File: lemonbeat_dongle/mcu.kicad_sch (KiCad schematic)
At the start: 43 parts, among them J201 USB_A, J202 Prog, J203 u.FL, SW201 SW_Push, U201 nRF52840, Y201 32MHz, Y202 32.768kHz

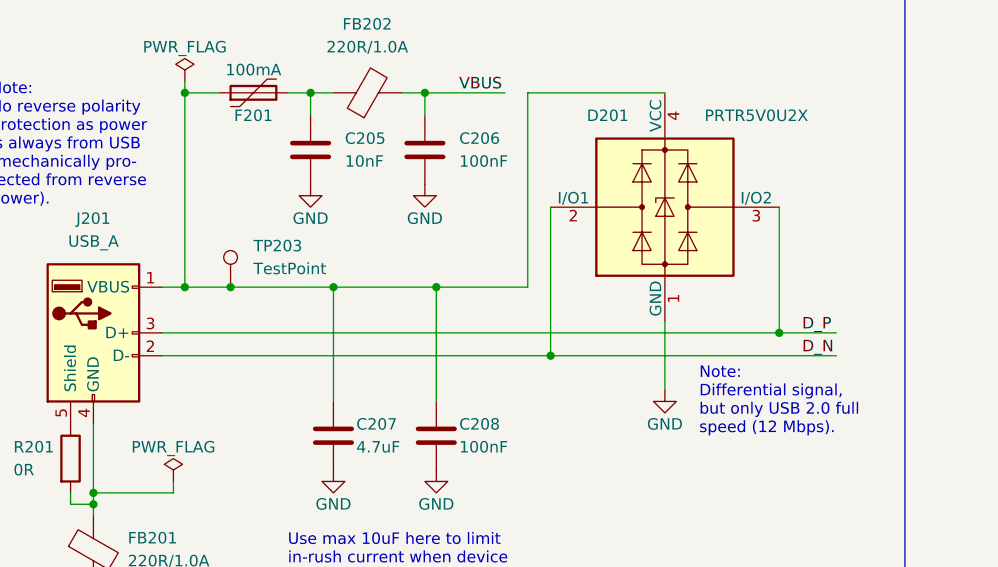
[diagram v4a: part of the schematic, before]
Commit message: dongle: schematic: switch ESD protection D_P/D_N to facilitate routing
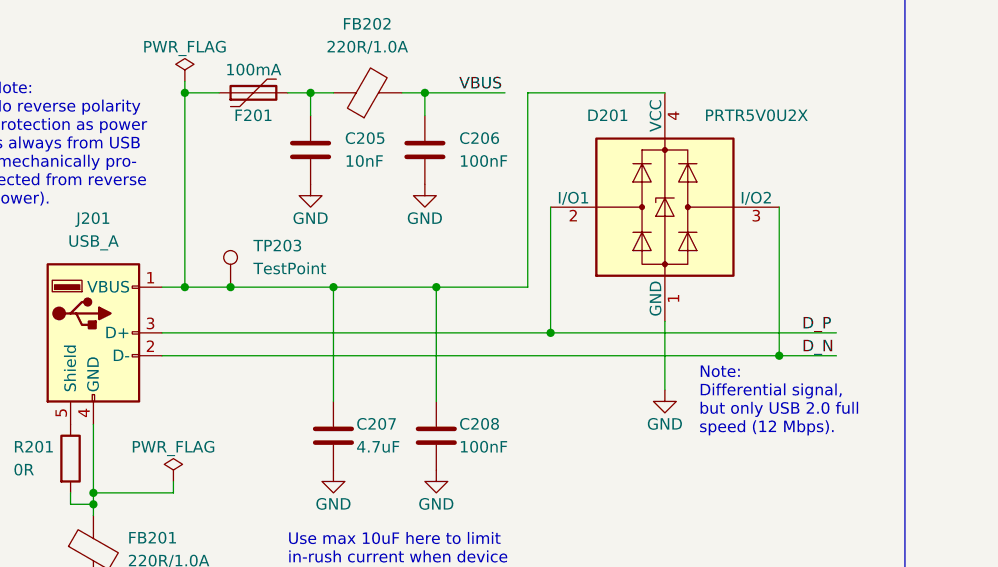
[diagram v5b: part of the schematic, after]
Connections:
- net D_N: now also D201.3 (I/O2); no longer D201.2 (I/O1)
- net D_P: now also D201.2 (I/O1); no longer D201.3 (I/O2)
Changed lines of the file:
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@@
   (junction (at 213.36 48.26) (diameter 0) (color 0 0 0 0)
   )
+  (junction (at 265.43 77.47) (diameter 0) (color 0 0 0 0)
+  )
   (junction (at 80.01 190.5) (diameter 0) (color 0 0 0 0)
   )
@@
   (junction (at 21.59 123.19) (diameter 0) (color 0 0 0 0)
   )
-  (junction (at 240.03 77.47) (diameter 0) (color 0 0 0 0)
-  )
   (junction (at 101.6 19.05) (diameter 0) (color 0 0 0 0)
   )
@@
   (junction (at 187.96 129.54) (diameter 0) (color 0 0 0 0)
   )
-  (junction (at 265.43 74.93) (diameter 0) (color 0 0 0 0)
-  )
   (junction (at 91.44 43.18) (diameter 0) (color 0 0 0 0)
   )
@@
   )
   (junction (at 237.49 138.43) (diameter 0) (color 0 0 0 0)
+  )
+  (junction (at 240.03 74.93) (diameter 0) (color 0 0 0 0)
   )
   (junction (at 97.79 19.05) (diameter 0) (color 0 0 0 0)
@@
     (stroke (width 0) (type default) (color 0 0 0 0))
   )
+  (wire (pts (xy 265.43 60.96) (xy 265.43 77.47))
+    (stroke (width 0) (type default) (color 0 0 0 0))
+  )
   (wire (pts (xy 71.12 39.37) (xy 71.12 46.99))
     (stroke (width 0) (type default) (color 0 0 0 0))
@@
     (stroke (width 0) (type default) (color 0 0 0 0))
   )
-  (wire (pts (xy 240.03 60.96) (xy 240.03 77.47))
-    (stroke (width 0) (type default) (color 0 0 0 0))
-  )
   (wire (pts (xy 43.18 121.92) (xy 43.18 123.19))
     (stroke (width 0) (type default) (color 0 0 0 0))
@@
     (stroke (width 0) (type default) (color 0 0 0 0))
   )
-  (wire (pts (xy 196.85 77.47) (xy 240.03 77.47))
-    (stroke (width 0) (type default) (color 0 0 0 0))
-  )
   (wire (pts (xy 227.33 69.85) (xy 237.49 69.85))
     (stroke (width 0) (type default) (color 0 0 0 0))
@@
     (stroke (width 0) (type default) (color 0 0 0 0))
   )
-  (wire (pts (xy 265.43 74.93) (xy 271.78 74.93))
+  (wire (pts (xy 196.85 74.93) (xy 240.03 74.93))
     (stroke (width 0) (type default) (color 0 0 0 0))
   )
@@
     (stroke (width 0) (type default) (color 0 0 0 0))
   )
-  (wire (pts (xy 196.85 74.93) (xy 265.43 74.93))
-    (stroke (width 0) (type default) (color 0 0 0 0))
-  )
   (wire (pts (xy 121.92 102.87) (xy 124.46 102.87))
     (stroke (width 0) (type default) (color 0 0 0 0))
@@
     (stroke (width 0) (type default) (color 0 0 0 0))
   )
-  (wire (pts (xy 265.43 60.96) (xy 265.43 74.93))
+  (wire (pts (xy 240.03 74.93) (xy 271.78 74.93))
     (stroke (width 0) (type default) (color 0 0 0 0))
   )
@@
     (stroke (width 0) (type default) (color 0 0 0 0))
   )
-  (wire (pts (xy 240.03 77.47) (xy 271.78 77.47))
+  (wire (pts (xy 196.85 77.47) (xy 265.43 77.47))
     (stroke (width 0) (type default) (color 0 0 0 0))
   )
@@
     (stroke (width 0) (type default) (color 0 0 0 0))
   )
+  (wire (pts (xy 240.03 60.96) (xy 240.03 74.93))
+    (stroke (width 0) (type default) (color 0 0 0 0))
+  )
   (wire (pts (xy 17.78 161.29) (xy 19.05 161.29))
     (stroke (width 0) (type default) (color 0 0 0 0))
@@
     (stroke (width 0) (type default) (color 0 0 0 0))
   )
+  (wire (pts (xy 265.43 77.47) (xy 271.78 77.47))
+    (stroke (width 0) (type default) (color 0 0 0 0))
+  )

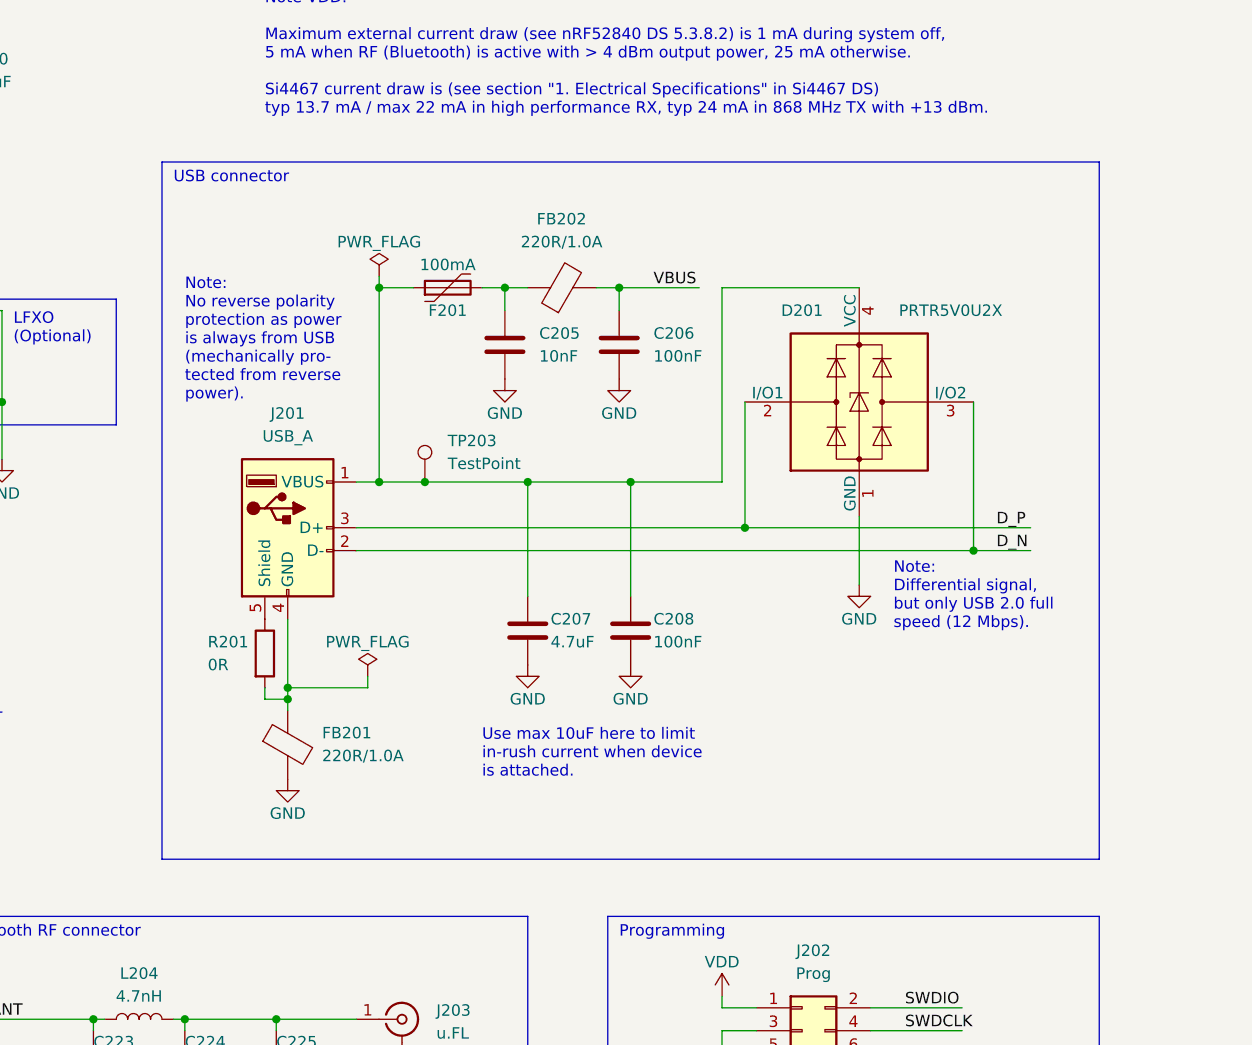
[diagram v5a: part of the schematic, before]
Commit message: dongle: schematic: move C207 after fuse & clean up USB schematic
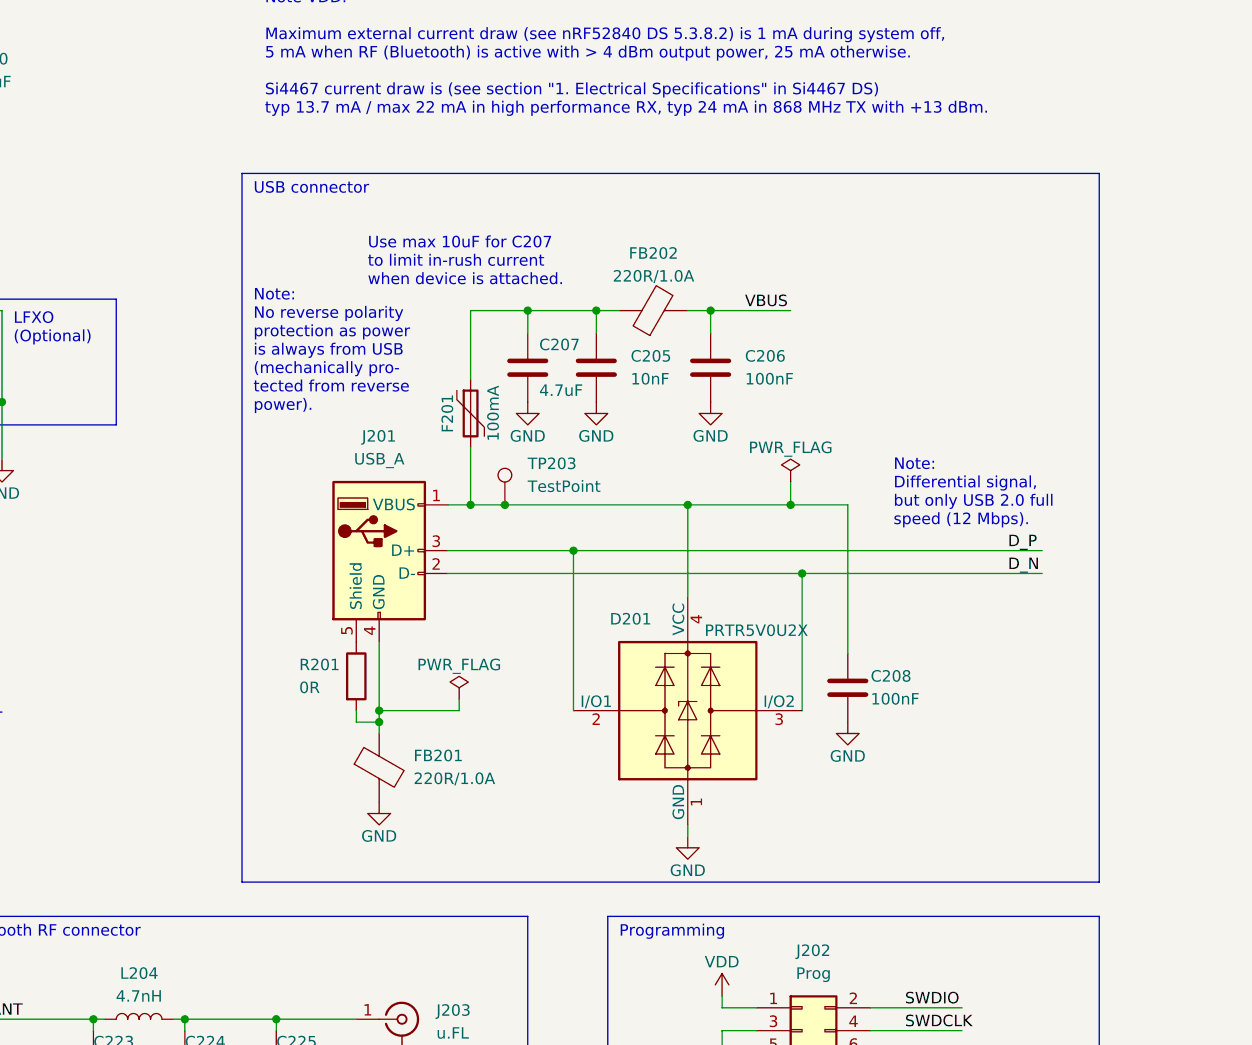
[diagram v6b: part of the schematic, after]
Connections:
- net at C208.1, D201.4 (VCC), J201.1 (VBUS)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: now also F201.2; no longer C207.1, F201.1
- net at C205.1, FB202.1: now also C207.1, F201.1; no longer F201.2
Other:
- note added: "Use max 10uF for C207 to limit in-rush current when device is attached."
- note removed: "Use max 10uF here to limit in-rush current when device is attached."
- moved on the sheet: C205, C206, C207, C208, D201, F201, FB201, FB202, J201, R201, TP203

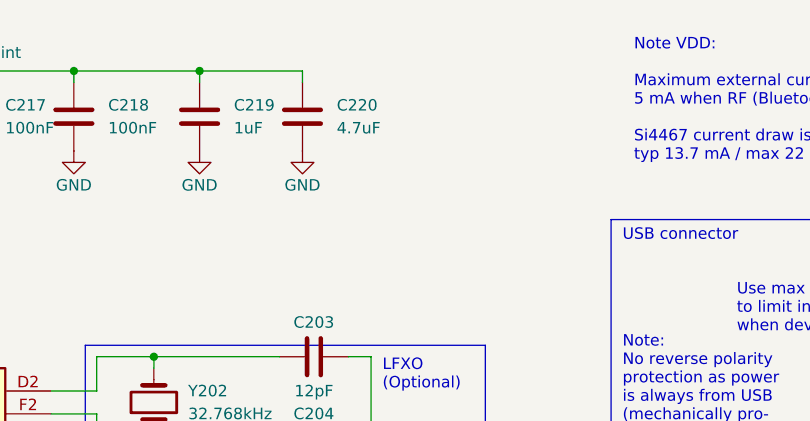
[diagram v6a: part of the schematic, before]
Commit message: dongle: schematic: add additional decoupling capacitor for nRF52840
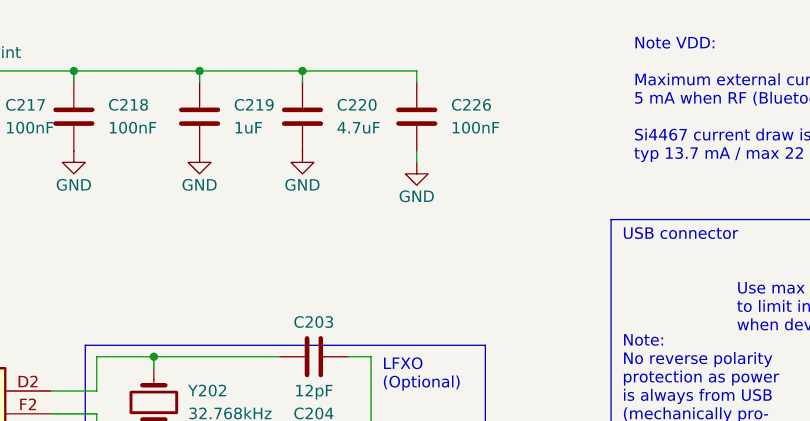
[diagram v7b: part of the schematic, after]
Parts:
- added C226: 100nF, Resistor_SMD:R_0201_0603Metric, symbol Device:C
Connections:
- net GND: now also C226.2
- net VDD: now also C226.1
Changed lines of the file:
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@@
   (junction (at 133.35 50.8) (diameter 0) (color 0 0 0 0)
+  )
+  (junction (at 149.86 19.05) (diameter 0) (color 0 0 0 0)
   )
   (junction (at 246.38 80.01) (diameter 0) (color 0 0 0 0)
@@
     (stroke (width 0) (type default) (color 0 0 0 0))
   )
+  (wire (pts (xy 149.86 19.05) (xy 162.56 19.05))
+    (stroke (width 0) (type default) (color 0 0 0 0))
+  )
   (wire (pts (xy 49.53 119.38) (xy 49.53 118.11))
     (stroke (width 0) (type default) (color 0 0 0 0))
@@
     (stroke (width 0) (type default) (color 0 0 0 0))
   )
+  (wire (pts (xy 162.56 27.94) (xy 162.56 29.21))
+    (stroke (width 0) (type default) (color 0 0 0 0))
+  )
   (wire (pts (xy 43.18 113.03) (xy 55.88 113.03))
     (stroke (width 0) (type default) (color 0 0 0 0))
@@
   )
   (wire (pts (xy 17.78 62.23) (xy 17.78 63.5))
+    (stroke (width 0) (type default) (color 0 0 0 0))
+  )
+  (wire (pts (xy 162.56 20.32) (xy 162.56 19.05))
     (stroke (width 0) (type default) (color 0 0 0 0))
   )
@@
     )
     (property "Part Number" "MGLB1005M221T1R0-LF " (id 8) (at 199.39 101.6 0)
+      (effects (font (size 1.27 1.27)) hide)
+    )
+    (pin "1")
+    (pin "2")
+  )
+  (symbol (lib_id "Device:C") (at 162.56 24.13 0) (unit 1)
+    (in_bom yes) (on_board yes) (fields_autoplaced)
+    (property "Reference" "C226" (id 0) (at 166.37 22.8599 0)
+      (effects (font (size 1.27 1.27)) (justify left))
+    )
+    (property "Value" "100nF" (id 1) (at 166.37 25.3999 0)
+      (effects (font (size 1.27 1.27)) (justify left))
+    )
+    (property "Footprint" "Resistor_SMD:R_0201_0603Metric" (id 2) (at 163.5252 27.94 0)
+      (effects (font (size 1.27 1.27)) hide)
+    )
+    (property "Datasheet" "~" (id 3) (at 162.56 24.13 0)
+      (effects (font (size 1.27 1.27)) hide)
+    )
+    (property "Description" "25V 100nF X5R ±10% 0201" (id 4) (at 162.56 24.13 0)
+      (effects (font (size 1.27 1.27)) hide)
+    )
+    (property "LCSC" "C76939" (id 5) (at 162.56 24.13 0)
+      (effects (font (size 1.27 1.27)) hide)
+    )
+    (property "Manufacturer" "Murata Electronics" (id 6) (at 162.56 24.13 0)
+      (effects (font (size 1.27 1.27)) hide)
+    )
+    (property "Part Number" "GRM033R61E104KE14D" (id 7) (at 162.56 24.13 0)
       (effects (font (size 1.27 1.27)) hide)
     )
@@
     (pin "Y23")
   )
+  (symbol (lib_id "power:GND") (at 162.56 29.21 0) (unit 1)
+    (in_bom yes) (on_board yes)
+    (property "Reference" "#PWR0233" (id 0) (at 162.56 35.56 0)
+      (effects (font (size 1.27 1.27)) hide)
+    )
+    (property "Value" "GND" (id 1) (at 162.56 33.02 0))
+    (property "Footprint" "" (id 2) (at 162.56 29.21 0)
+      (effects (font (size 1.27 1.27)) hide)
+    )
+    (property "Datasheet" "" (id 3) (at 162.56 29.21 0)
+      (effects (font (size 1.27 1.27)) hide)
+    )
+    (pin "1")
+  )
   (symbol (lib_id "power:GND") (at 19.05 92.71 0) (unit 1)
